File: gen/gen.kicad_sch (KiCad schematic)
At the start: 16 parts

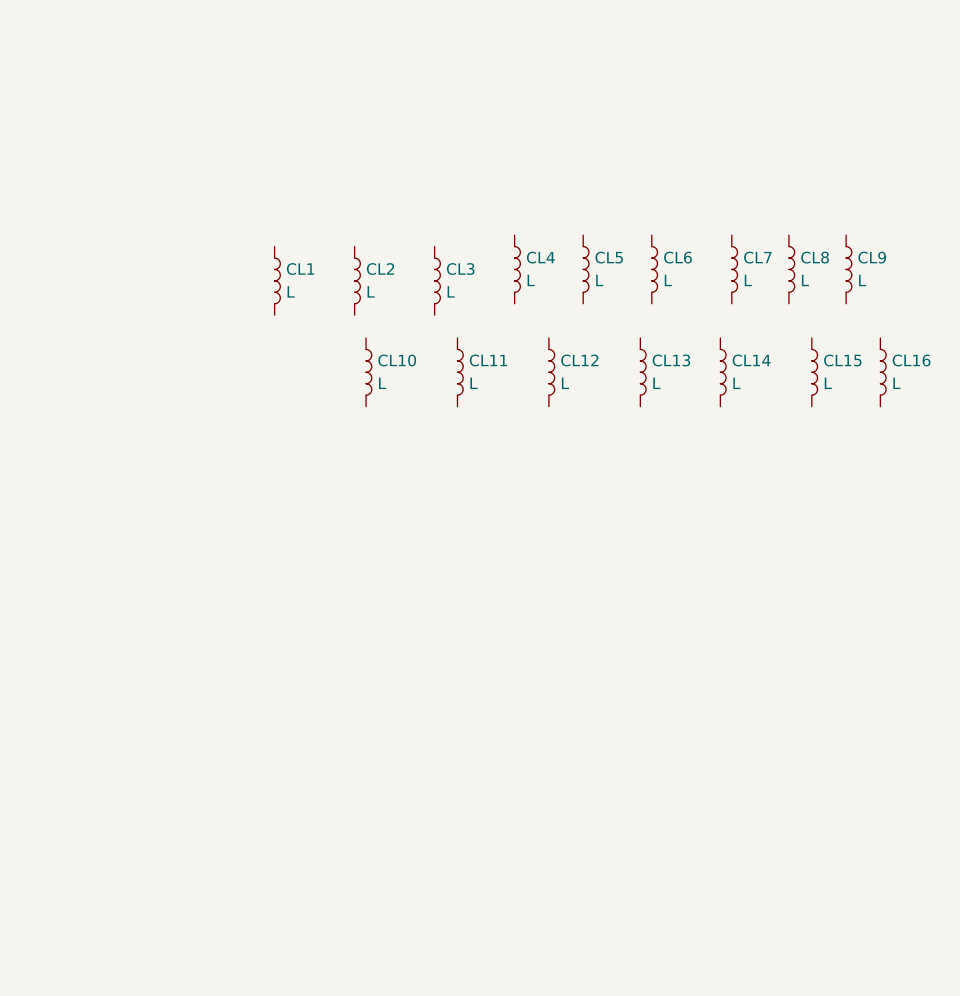
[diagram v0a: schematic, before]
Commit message: Added 6 layer coils
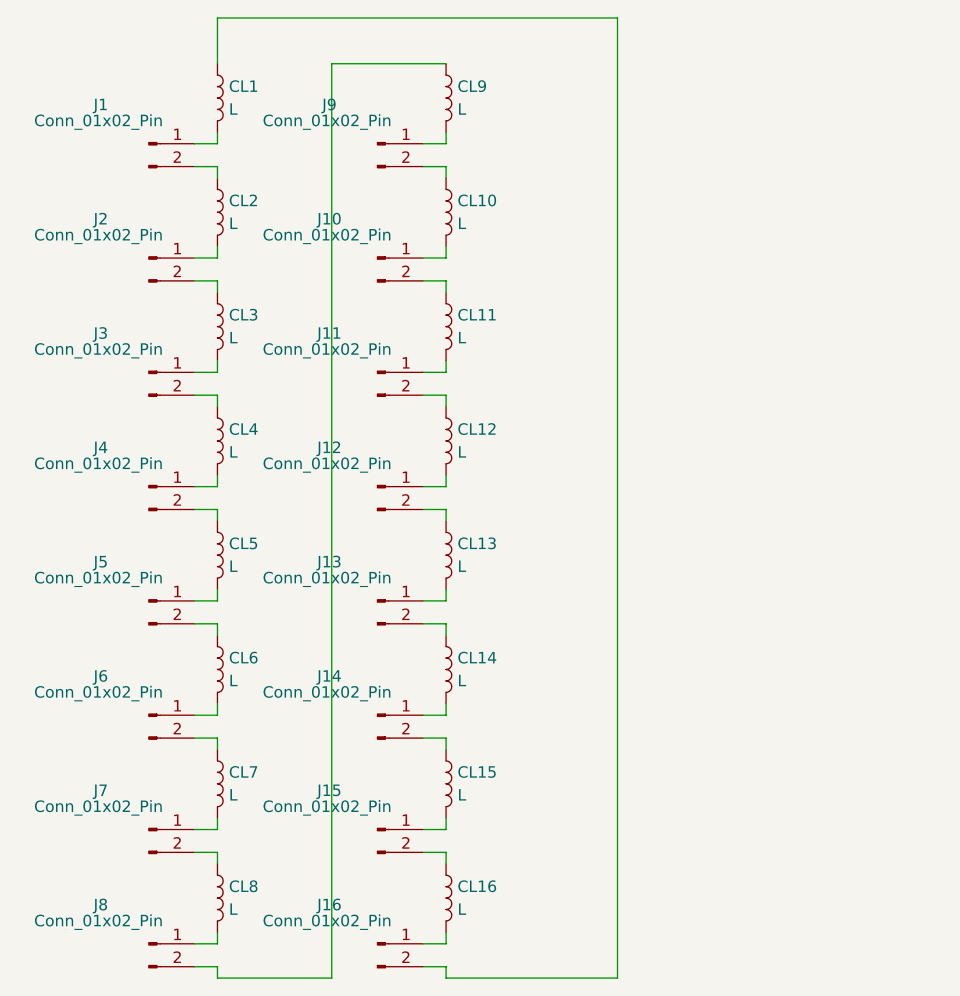
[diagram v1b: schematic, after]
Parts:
- added J1, J10, J11, J12, J13, J14, J15, J16, J2, J3, J4, J5, J6, J7, J8, J9: Conn_01x02_Pin, Jumper:SolderJumper-2_P1.3mm_Open_RoundedPad1.0x1.5mm, symbol Connector:Conn_01x02_Pin
- CL1, CL10, CL11, CL12, CL13, CL14, CL15, CL16, CL2, CL3, CL4, CL5, CL6, CL7, CL8, CL9: footprint (none) -> PCB Coils:SMALL_COIL_6
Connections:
- net at CL5.1: now also J4.2 (Pin_2)
- net at CL5.2: now also J5.1 (Pin_1)
- net at CL14.1: now also J13.2 (Pin_2)
- net at CL14.2: now also J14.1 (Pin_1)
- net at CL15.1: now also J14.2 (Pin_2)
- net at CL15.2: now also J15.1 (Pin_1)
- net at CL7.1: now also J6.2 (Pin_2)
- net at CL7.2: now also J7.1 (Pin_1)
- net at CL2.1: now also J1.2 (Pin_2)
- net at CL2.2: now also J2.1 (Pin_1)
- net at CL12.1: now also J11.2 (Pin_2)
- net at CL12.2: now also J12.1 (Pin_1)
- net at CL13.1: now also J12.2 (Pin_2)
- net at CL13.2: now also J13.1 (Pin_1)
- net at CL1.1: now also J16.2 (Pin_2)
- net at CL1.2: now also J1.1 (Pin_1)
- net at CL3.1: now also J2.2 (Pin_2)
- net at CL3.2: now also J3.1 (Pin_1)
- net at CL9.1: now also J8.2 (Pin_2)
- net at CL9.2: now also J9.1 (Pin_1)
- net at CL8.1: now also J7.2 (Pin_2)
- net at CL8.2: now also J8.1 (Pin_1)
- net at CL4.1: now also J3.2 (Pin_2)
- net at CL4.2: now also J4.1 (Pin_1)
- net at CL10.1: now also J9.2 (Pin_2)
- net at CL10.2: now also J10.1 (Pin_1)
- net at CL11.1: now also J10.2 (Pin_2)
- net at CL11.2: now also J11.1 (Pin_1)
- net at CL6.1: now also J5.2 (Pin_2)
- net at CL6.2: now also J6.1 (Pin_1)
- net at CL16.1: now also J15.2 (Pin_2)
- net at CL16.2: now also J16.1 (Pin_1)
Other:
- moved on the sheet: CL1, CL10, CL11, CL12, CL13, CL14, CL15, CL16, CL2, CL3, CL4, CL5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
